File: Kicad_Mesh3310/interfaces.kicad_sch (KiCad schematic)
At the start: 52 parts, among them J5 Vibrator, J6 Buzzer, J7 Display, Q4 BSS138, Q5 BSS138, Q6 IRLML6401, Q7 BSS138

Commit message: Cleaning and placing
Cleaning and placing components
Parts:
- D10, D11, D12, D13, D5, D6, D7, D9: footprint Parts:3310_led -> mesh3310_footprints:3310_led
- J5: footprint Parts:3310_vibrator -> mesh3310_footprints:3310_vibrator
- J6: footprint Parts:3310_buzzer -> mesh3310_footprints:3310_buzzer
- J7: footprint Parts:3310_display -> mesh3310_footprints:3310_display
- SW10, SW11, SW12, SW13, SW14, SW15, SW17, SW3, SW4, SW5, SW6, SW7, SW8, SW9: footprint Parts:3310_key -> mesh3310_footprints:3310_key
- SW16: footprint Parts:3310_key_gap -> mesh3310_footprints:3310_key_gap
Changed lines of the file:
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@@
 			)
 		)
-		(property "Footprint" "Parts:3310_key"
+		(property "Footprint" "mesh3310_footprints:3310_key"
 			(at 99.06 105.41 0)
 			(effects
@@
 			)
 		)
-		(property "Footprint" "Parts:3310_led"
+		(property "Footprint" "mesh3310_footprints:3310_led"
 			(at 60.96 176.53 0)
 			(effects
@@
 			)
 		)
-		(property "Footprint" "Parts:3310_key"
+		(property "Footprint" "mesh3310_footprints:3310_key"
 			(at 111.76 105.41 0)
 			(effects
@@
 			)
 		)
-		(property "Footprint" "Parts:3310_led"
+		(property "Footprint" "mesh3310_footprints:3310_led"
 			(at 105.41 176.53 0)
 			(effects
@@
 			)
 		)
-		(property "Footprint" "Parts:3310_key"
+		(property "Footprint" "mesh3310_footprints:3310_key"
 			(at 111.76 85.09 0)
 			(effects
@@
 			)
 		)
-		(property "Footprint" "Parts:3310_led"
+		(property "Footprint" "mesh3310_footprints:3310_led"
 			(at 114.3 176.53 0)
 			(effects
@@
 			)
 		)
-		(property "Footprint" "Parts:3310_display"
+		(property "Footprint" "mesh3310_footprints:3310_display"
 			(at 233.68 105.41 0)
 			(effects
@@
 			)
 		)
-		(property "Footprint" "Parts:3310_key"
+		(property "Footprint" "mesh3310_footprints:3310_key"
 			(at 99.06 74.93 0)
 			(effects
@@
 			)
 		)
-		(property "Footprint" "Parts:3310_key"
+		(property "Footprint" "mesh3310_footprints:3310_key"
 			(at 99.06 85.09 0)
 			(effects
@@
 			)
 		)
-		(property "Footprint" "Parts:3310_key"
+		(property "Footprint" "mesh3310_footprints:3310_key"
 			(at 99.06 115.57 0)
 			(effects
@@
 			)
 		)
-		(property "Footprint" "Parts:3310_key_gap"
+		(property "Footprint" "mesh3310_footprints:3310_key_gap"
 			(at 124.46 105.41 0)
 			(effects
@@
 			)
 		)
-		(property "Footprint" "Parts:3310_key"
+		(property "Footprint" "mesh3310_footprints:3310_key"
 			(at 111.76 95.25 0)
 			(effects
@@
 			)
 		)
-		(property "Footprint" "Parts:3310_key"
+		(property "Footprint" "mesh3310_footprints:3310_key"
 			(at 99.06 95.25 0)
 			(effects
@@
 			)
 		)
-		(property "Footprint" "Parts:3310_led"
+		(property "Footprint" "mesh3310_footprints:3310_led"
 			(at 69.85 176.53 0)
 			(effects
@@
 			)
 		)
-		(property "Footprint" "Parts:3310_led"
+		(property "Footprint" "mesh3310_footprints:3310_led"
 			(at 123.19 176.53 0)
 			(effects
@@
 			)
 		)
-		(property "Footprint" "Parts:3310_key"
+		(property "Footprint" "mesh3310_footprints:3310_key"
 			(at 124.46 115.57 0)
 			(effects
@@
 			)
 		)
-		(property "Footprint" "Parts:3310_key"
+		(property "Footprint" "mesh3310_footprints:3310_key"
 			(at 111.76 115.57 0)
 			(effects
@@
 			)
 		)
-		(property "Footprint" "Parts:3310_key"
+		(property "Footprint" "mesh3310_footprints:3310_key"
 			(at 111.76 74.93 0)
 			(effects
@@
 			)
 		)
-		(property "Footprint" "Parts:3310_vibrator"
+		(property "Footprint" "mesh3310_footprints:3310_vibrator"
 			(at 212.09 41.91 0)
 			(effects
@@
 			)
 		)
-		(property "Footprint" "Parts:3310_led"
+		(property "Footprint" "mesh3310_footprints:3310_led"
 			(at 96.52 176.53 0)
 			(effects
@@
 			)
 		)
-		(property "Footprint" "Parts:3310_buzzer"
+		(property "Footprint" "mesh3310_footprints:3310_buzzer"
 			(at 246.38 41.91 0)
 			(effects
@@
 			)
 		)
-		(property "Footprint" "Parts:3310_key"
+		(property "Footprint" "mesh3310_footprints:3310_key"
 			(at 124.46 74.93 0)
 			(effects
@@
 			)
 		)
-		(property "Footprint" "Parts:3310_led"
+		(property "Footprint" "mesh3310_footprints:3310_led"
 			(at 78.74 176.53 0)
 			(effects
@@
 			)
 		)
-		(property "Footprint" "Parts:3310_key"
+		(property "Footprint" "mesh3310_footprints:3310_key"
 			(at 124.46 85.09 0)
 			(effects
@@
 			)
 		)
-		(property "Footprint" "Parts:3310_key"
+		(property "Footprint" "mesh3310_footprints:3310_key"
 			(at 124.46 95.25 0)
 			(effects
@@
 			)
 		)
-		(property "Footprint" "Parts:3310_led"
+		(property "Footprint" "mesh3310_footprints:3310_led"
 			(at 87.63 176.53 0)
 			(effects

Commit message: RF designing
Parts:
- C16, C17: footprint Capacitor_Tantalum_SMD:CP_EIA-3528-21_Kemet-B -> Capacitor_Tantalum_SMD:CP_EIA-1608-08_AVX-J
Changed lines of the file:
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@@
 			)
 		)
-		(property "Footprint" "Capacitor_Tantalum_SMD:CP_EIA-3528-21_Kemet-B"
+		(property "Footprint" "Capacitor_Tantalum_SMD:CP_EIA-1608-08_AVX-J"
 			(at 229.5652 135.89 0)
 			(effects
@@
 			)
 		)
-		(property "Footprint" "Capacitor_Tantalum_SMD:CP_EIA-3528-21_Kemet-B"
+		(property "Footprint" "Capacitor_Tantalum_SMD:CP_EIA-1608-08_AVX-J"
 			(at 248.6152 125.73 0)
 			(effects

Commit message: cleanup
schematic cleanup
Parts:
- added R47, R48: 10k, Resistor_SMD:R_0402_1005Metric, symbol symbols:R
- added TP1: 3.3v, TestPoint:TestPoint_Pad_D1.5mm, symbol Connector:TestPoint
- added TP2: GND, TestPoint:TestPoint_Pad_D1.5mm, symbol Connector:TestPoint
- added TP3: SDA, TestPoint:TestPoint_Pad_D1.5mm, symbol Connector:TestPoint
- added TP4: SCL, TestPoint:TestPoint_Pad_D1.5mm, symbol Connector:TestPoint
- added U11: USBLC6-2P6, Package_TO_SOT_SMD:SOT-666, symbol Power_Protection:USBLC6-2P6
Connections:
- net +3V3: now also R47.2, R48.2, TP1.1, U11.5 (VBUS)
- net GND: now also TP2.1, U11.2 (GND)
- new net: TP4.1, U11.3 (I/O2)
- new net: TP3.1, U11.1 (I/O1)
- new net SCL: R48.1, U11.4 (I/O2)
- new net SDA: R47.1, U11.6 (I/O1)
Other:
- moved on the sheet: R31, R32, R33, R34, R35, SW10, SW11, SW12, SW13, SW14, SW15, SW16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

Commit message: Lora antenna replacement
Lora antenna replacement, added Nordic nRF 9151 for GPS , VoIP ,VoLTE-m , SIP
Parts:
- R15, R16, R17, R18, R19, R20, R21, R22, R23, R24, R25, R26, R27, R31, R32, R33, R34, R35, R47, R48: footprint Resistor_SMD:R_0402_1005Metric -> Resistor_SMD:R_0201_0603Metric
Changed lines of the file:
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@@
 			)
 		)
-		(property "Footprint" "Resistor_SMD:R_0402_1005Metric"
+		(property "Footprint" "Resistor_SMD:R_0201_0603Metric"
 			(at 38.1 173.228 90)
 			(effects
@@
 			)
 		)
-		(property "Footprint" "Resistor_SMD:R_0402_1005Metric"
+		(property "Footprint" "Resistor_SMD:R_0201_0603Metric"
 			(at 76.962 166.37 90)
 			(effects
@@
 			)
 		)
-		(property "Footprint" "Resistor_SMD:R_0402_1005Metric"
+		(property "Footprint" "Resistor_SMD:R_0201_0603Metric"
 			(at 82.55 62.992 90)
 			(effects
@@
 			)
 		)
-		(property "Footprint" "Resistor_SMD:R_0402_1005Metric"
+		(property "Footprint" "Resistor_SMD:R_0201_0603Metric"
 			(at 184.658 83.82 90)
 			(effects
@@
 			)
 		)
-		(property "Footprint" "Resistor_SMD:R_0402_1005Metric"
+		(property "Footprint" "Resistor_SMD:R_0201_0603Metric"
 			(at 177.038 83.82 90)
 			(effects
@@
 			)
 		)
-		(property "Footprint" "Resistor_SMD:R_0402_1005Metric"
+		(property "Footprint" "Resistor_SMD:R_0201_0603Metric"
 			(at 94.742 166.37 90)
 			(effects
@@
 			)
 		)
-		(property "Footprint" "Resistor_SMD:R_0402_1005Metric"
+		(property "Footprint" "Resistor_SMD:R_0201_0603Metric"
 			(at 103.632 166.37 90)
 			(effects
@@
 			)
 		)
-		(property "Footprint" "Resistor_SMD:R_0402_1005Metric"
+		(property "Footprint" "Resistor_SMD:R_0201_0603Metric"
 			(at 212.598 60.96 90)
 			(effects
@@
 			)
 		)
-		(property "Footprint" "Resistor_SMD:R_0402_1005Metric"
+		(property "Footprint" "Resistor_SMD:R_0201_0603Metric"
 			(at 68.072 166.37 90)
 			(effects
@@
 			)
 		)
-		(property "Footprint" "Resistor_SMD:R_0402_1005Metric"
+		(property "Footprint" "Resistor_SMD:R_0201_0603Metric"
 			(at 82.55 83.312 90)
 			(effects
@@
 			)
 		)
-		(property "Footprint" "Resistor_SMD:R_0402_1005Metric"
+		(property "Footprint" "Resistor_SMD:R_0201_0603Metric"
 			(at 82.55 103.632 90)
 			(effects
@@
 			)
 		)
-		(property "Footprint" "Resistor_SMD:R_0402_1005Metric"
+		(property "Footprint" "Resistor_SMD:R_0201_0603Metric"
 			(at 112.522 166.37 90)
 			(effects
@@
 			)
 		)
-		(property "Footprint" "Resistor_SMD:R_0402_1005Metric"
+		(property "Footprint" "Resistor_SMD:R_0201_0603Metric"
 			(at 85.852 166.37 90)
 			(effects
@@
 			)
 		)
-		(property "Footprint" "Resistor_SMD:R_0402_1005Metric"
+		(property "Footprint" "Resistor_SMD:R_0201_0603Metric"
 			(at 121.412 166.37 90)
 			(effects
@@
 			)
 		)
-		(property "Footprint" "Resistor_SMD:R_0402_1005Metric"
+		(property "Footprint" "Resistor_SMD:R_0201_0603Metric"
 			(at 246.888 60.96 90)
 			(effects
@@
 			)
 		)
-		(property "Footprint" "Resistor_SMD:R_0402_1005Metric"
+		(property "Footprint" "Resistor_SMD:R_0201_0603Metric"
 			(at 82.55 93.472 90)
 			(effects
@@
 			)
 		)
-		(property "Footprint" "Resistor_SMD:R_0402_1005Metric"
+		(property "Footprint" "Resistor_SMD:R_0201_0603Metric"
 			(at 53.848 147.32 90)
 			(effects
@@
 			)
 		)
-		(property "Footprint" "Resistor_SMD:R_0402_1005Metric"
+		(property "Footprint" "Resistor_SMD:R_0201_0603Metric"
 			(at 82.55 73.152 90)
 			(effects
@@
 			)
 		)
-		(property "Footprint" "Resistor_SMD:R_0402_1005Metric"
+		(property "Footprint" "Resistor_SMD:R_0201_0603Metric"
 			(at 44.958 177.8 90)
 			(effects
@@
 			)
 		)
-		(property "Footprint" "Resistor_SMD:R_0402_1005Metric"
+		(property "Footprint" "Resistor_SMD:R_0201_0603Metric"
 			(at 59.182 166.37 90)
 			(effects

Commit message: Backing up work
Backup work for today
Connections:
- net COL_1 renamed P0.16_COL_1
- net COL_2 renamed P0.17_COL_2
- net COL_3 renamed P0.18_COL_3
- net ROW_1 renamed P1.01_ROW_1
- net ROW_2 renamed P1.02_ROW_2
- net ROW_3 renamed P1.03_ROW_3
- net ROW_4 renamed P1.04_ROW_4
- net ROW_5 renamed P1.05_ROW_5
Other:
- moved on the sheet: R31, R32, R33, R34, R35

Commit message: Backup work
Adding some extra pads
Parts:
- removed R47, R48: 10k, Resistor_SMD:R_0201_0603Metric, symbol symbols:R
- removed TP1: 3.3v, TestPoint:TestPoint_Pad_D1.5mm, symbol Connector:TestPoint
- removed TP2: GND, TestPoint:TestPoint_Pad_D1.5mm, symbol Connector:TestPoint
- removed TP3: SDA, TestPoint:TestPoint_Pad_D1.5mm, symbol Connector:TestPoint
- removed TP4: SCL, TestPoint:TestPoint_Pad_D1.5mm, symbol Connector:TestPoint
- removed U11: USBLC6-2P6, Package_TO_SOT_SMD:SOT-666, symbol Power_Protection:USBLC6-2P6
- added J2: Mic, mesh3310_footprints:3310_mic, symbol Connector:Conn_01x02_Pin

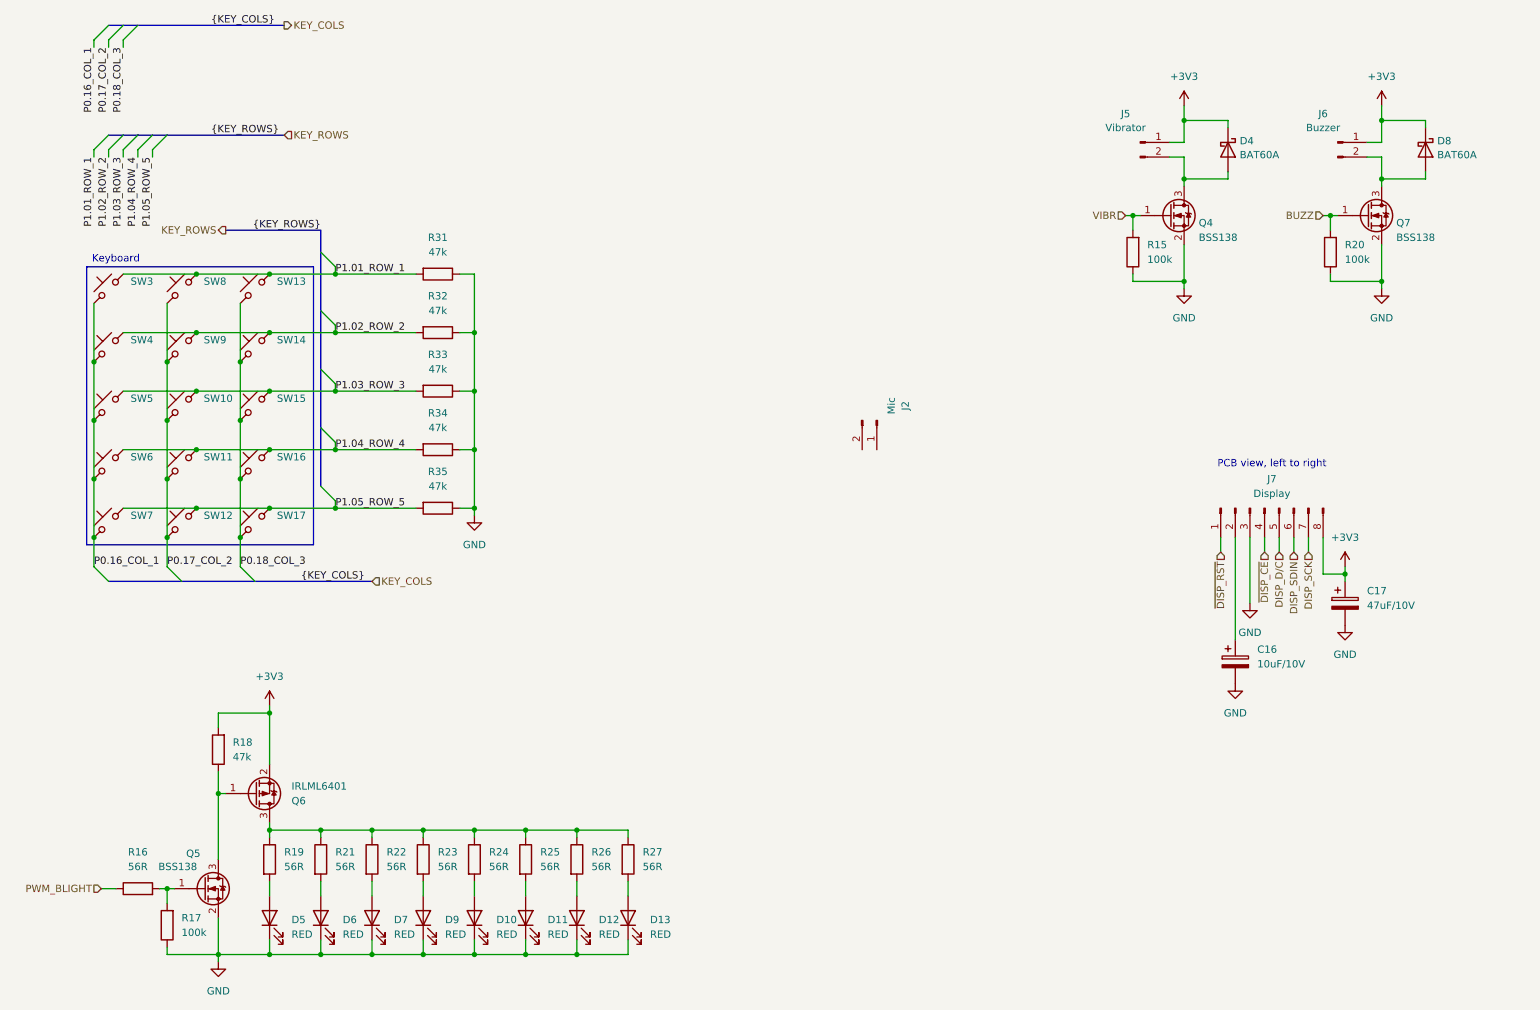
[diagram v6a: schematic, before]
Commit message: Schematic changes
Adding gsm module , interfaces : mic+earspeaker
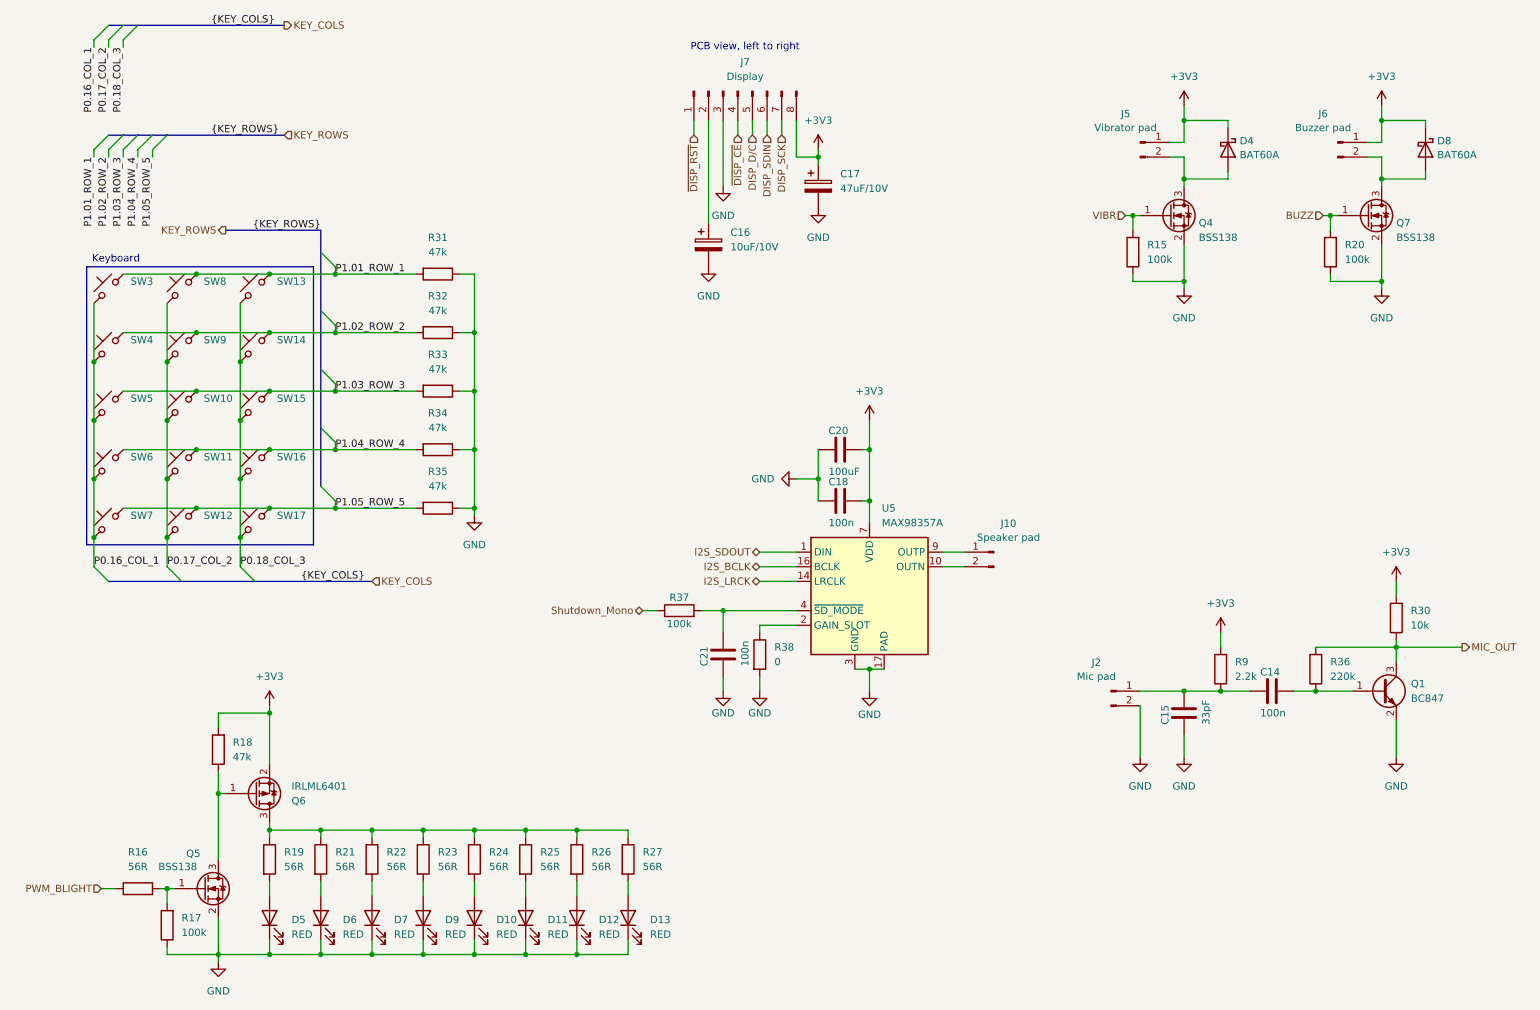
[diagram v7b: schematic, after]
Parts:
- added C14, C18, C21: 100n, Capacitor_SMD:C_0201_0603Metric, symbol Device:C
- added C15: 33pF, Capacitor_SMD:C_0201_0603Metric, symbol Device:C
- added C20: 100uF, Capacitor_SMD:C_0201_0603Metric, symbol Device:C
- added J10: Speaker pad, mesh3310_footprints:3310_earspeaker, symbol Connector:Conn_01x02_Pin
- added Q1: BC847, Package_TO_SOT_SMD:SOT-23, symbol Transistor_BJT:BC847
- added R30: 10k, Resistor_SMD:R_0201_0603Metric, symbol Device:R
- added R36: 220k, Resistor_SMD:R_0201_0603Metric, symbol Device:R
- added R37: 100k, Resistor_SMD:R_0201_0603Metric, symbol Device:R
- added R38: 0, Resistor_SMD:R_0201_0603Metric, symbol Device:R
- added R9: 2.2k, Resistor_SMD:R_0201_0603Metric, symbol Device:R
- added U5: MAX98357A, Package_DFN_QFN:TQFN-16-1EP_3x3mm_P0.5mm_EP1.23x1.23mm, symbol Audio:MAX98357A
- J2: value Mic -> Mic pad
- J5: value Vibrator -> Vibrator pad
- J6: value Buzzer -> Buzzer pad
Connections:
- net +3V3: now also C18.2, C20.2, R30.2, R9.2, U5.7 (VDD), U5.8 (VDD)
- net GND: now also J2.2 (Pin_2), C15.1, C18.1, C20.1, C21.1, Q1.2 (E), R38.2, U5.11 (GND), U5.15 (GND), U5.17 (PAD), U5.3 (GND)
- net at J2.1 (Pin_1): now also C14.1, C15.2, R9.1
- new net: C14.2, Q1.1 (B), R36.1
- new net: J10.2 (Pin_2), U5.10 (OUTN)
- new net: R38.1, U5.2 (GAIN_SLOT)
- new net: C21.2, R37.2, U5.4 (~{SD_MODE})
- new net: J10.1 (Pin_1), U5.9 (OUTP)
- new net I2S_BCLK: U5.16 (BCLK)
- new net I2S_LRCK: U5.14 (LRCLK)
- new net I2S_SDOUT: U5.1 (DIN)
- new net MIC_OUT: Q1.3 (C), R30.1, R36.2
- new net Shutdown_Mono: R37.1
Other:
- moved on the sheet: C16, C17, J2, J7
